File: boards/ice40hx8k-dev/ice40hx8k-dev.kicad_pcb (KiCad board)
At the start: 4 copper layers, 35 x 30 mm, 33 parts, among them U1 ICE40HX8K-CT256

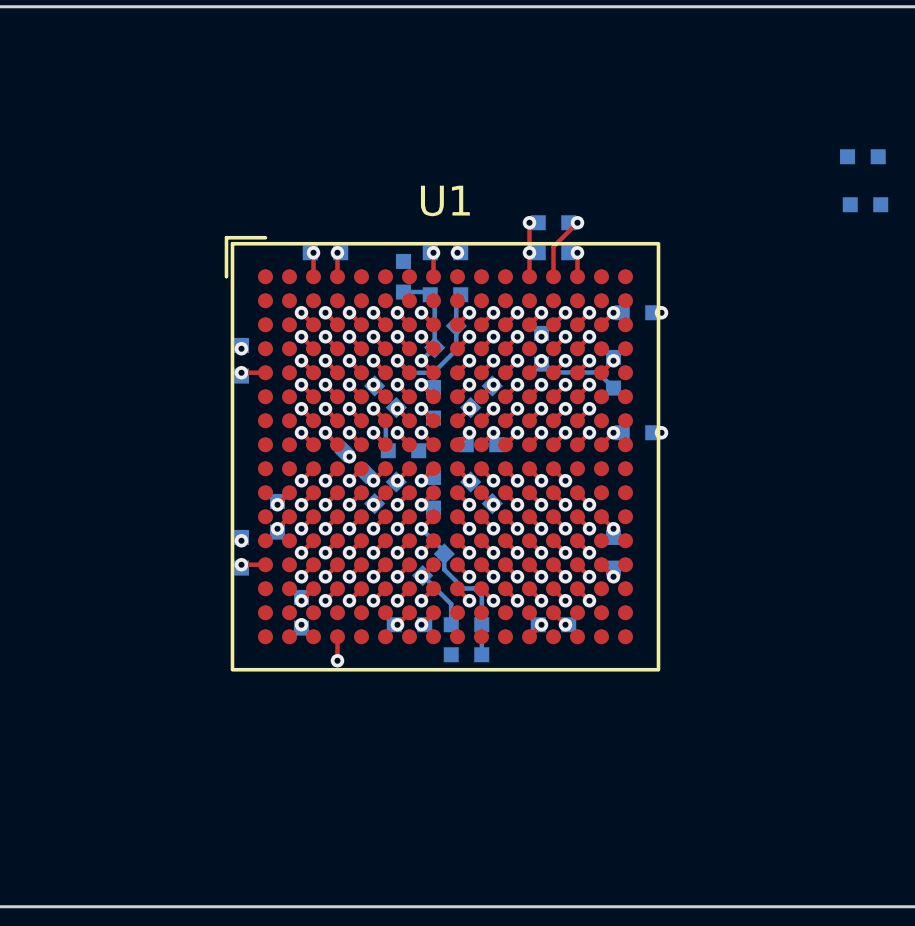
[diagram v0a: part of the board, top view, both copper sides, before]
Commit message: Fan out all signal pads.
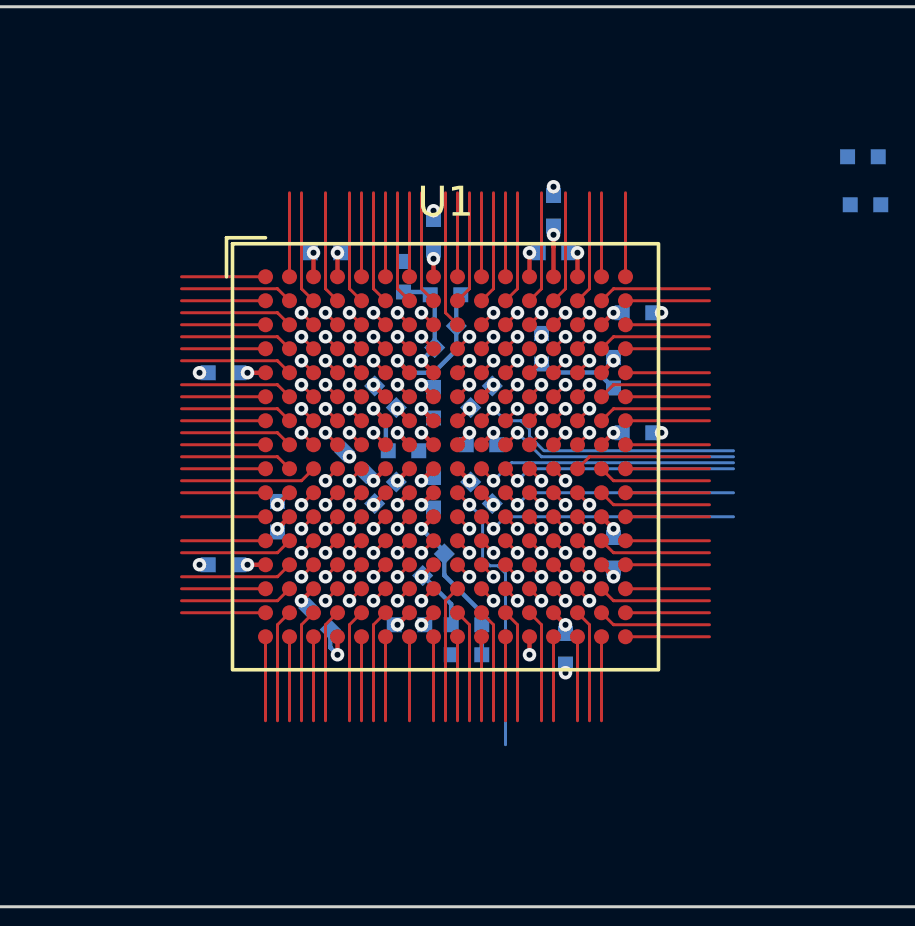
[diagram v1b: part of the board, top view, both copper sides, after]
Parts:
- moved C17 0.89 mm to (142.0, 91.4), turned to -90 degrees
- moved C24 0.72 mm to (137.6, 77.6), turned to 90 degrees
- moved C12 0.72 mm to (130.6, 82.2), turned to 180 degrees
- moved C13 0.72 mm to (130.6, 88.6), turned to 180 degrees
- moved C16 0.63 mm to (133.8, 90.4), turned to -45 degrees
- moved C25 0.40 mm to (141.6, 76.8), turned to 90 degrees
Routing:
- net unconnected-(U1-PadL6): track 0.57 -> 10.1 mm
- net unconnected-(U1-PadF5): track 0.57 -> 9.93 mm
- net unconnected-(U1-PadG10): track 0.57 -> 9.28 mm
- net unconnected-(U1-PadK9): track 0.57 -> 9.22 mm
- net unconnected-(U1-PadF7): track 0.57 -> 9.21 mm
- net unconnected-(U1-PadJ10): track 0.57 -> 8.81 mm
- net unconnected-(U1-PadL10): track 0.57 -> 8.73 mm
- net unconnected-(U1-PadL7): track 0.57 -> 8.50 mm
- net unconnected-(U1-PadL11): track 0.57 -> 8.45 mm
- net unconnected-(U1-PadG11): track 0.57 -> 8.38 mm
- net unconnected-(U1-PadE6): track 0.57 -> 8.33 mm
- net unconnected-(U1-PadF12): track 0.57 -> 8.21 mm
- net unconnected-(U1-PadH11): track 0.57 -> 8.10 mm
- net unconnected-(U1-PadM11): track 0.57 -> 8.08 mm
- net unconnected-(U1-PadK11): track 0.57 -> 7.93 mm
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
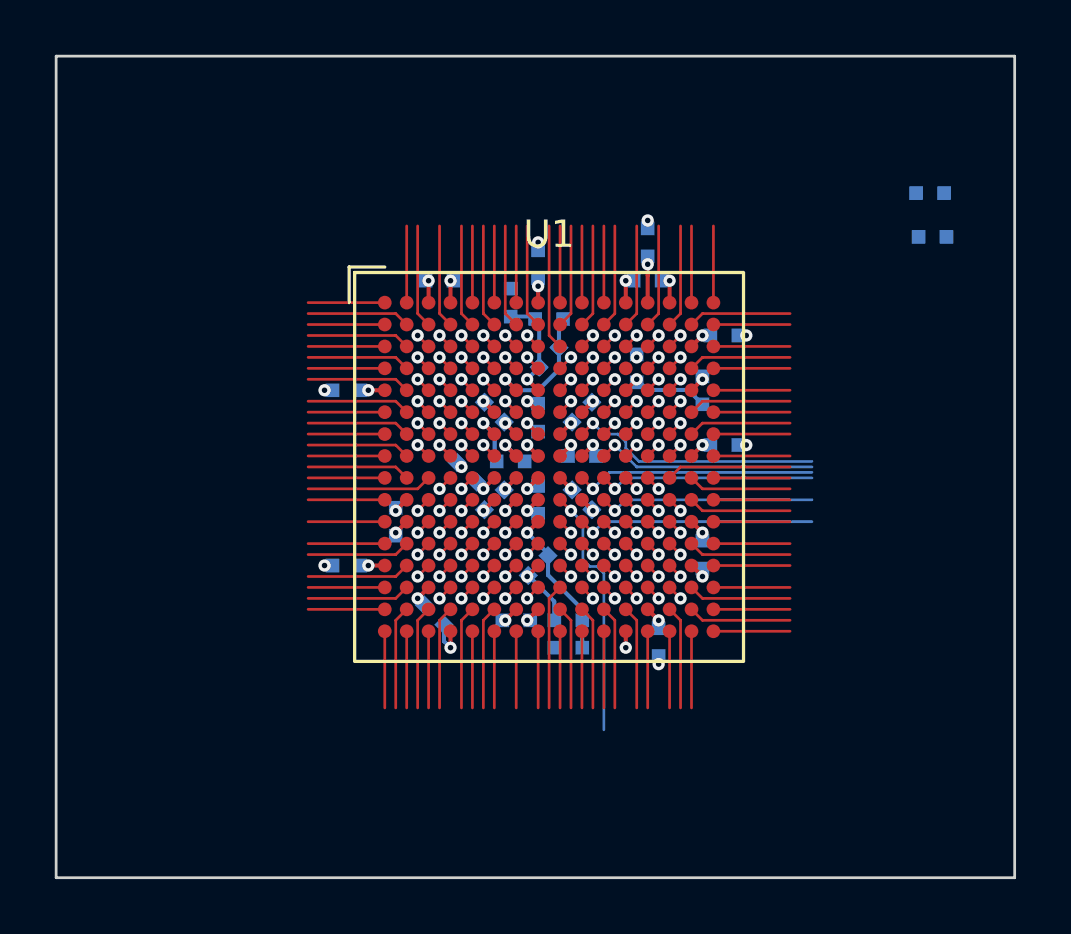
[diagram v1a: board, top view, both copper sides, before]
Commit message: Split up schematic and label all nets.
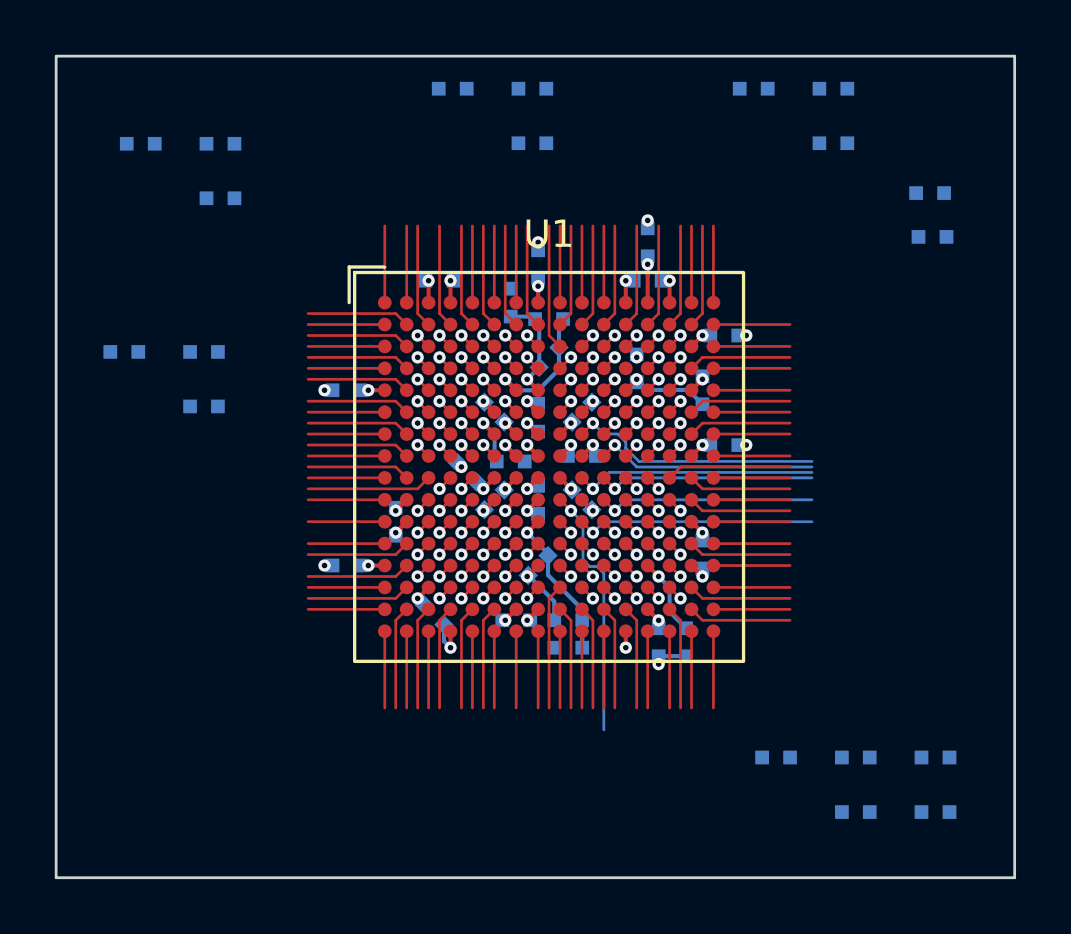
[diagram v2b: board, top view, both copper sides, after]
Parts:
- added C31: 100n, 0Local:C_SMD_0402_Pad0.5mm, B.Cu at (143.0, 91.4)
- added C32: 10n, 0Local:C_SMD_0402_Pad0.5mm, B.Cu at (149.2, 95.6)
- added C33: 10n, 0Local:C_SMD_0402_Pad0.5mm, B.Cu at (149.2, 97.6)
- added C34: 1u, 0Local:C_SMD_0402_Pad0.5mm, B.Cu at (146.3, 95.6)
- added C35: 10n, 0Local:C_SMD_0402_Pad0.5mm, B.Cu at (126.0, 73.2)
- added C36: 1u, 0Local:C_SMD_0402_Pad0.5mm, B.Cu at (126.0, 75.2)
- added C37: 10u, 0Local:C_SMD_0402_Pad0.5mm, B.Cu at (123.1, 73.2)
- added C38: 10n, 0Local:C_SMD_0402_Pad0.5mm, B.Cu at (125.4, 80.8)
- added C39: 1u, 0Local:C_SMD_0402_Pad0.5mm, B.Cu at (125.4, 82.8)
- added C40: 100n, 0Local:C_SMD_0402_Pad0.5mm, B.Cu at (122.5, 80.8)
- added C41: 10n, 0Local:C_SMD_0402_Pad0.5mm, B.Cu at (145.5, 71.2)
- added C42: 1u, 0Local:C_SMD_0402_Pad0.5mm, B.Cu at (148.4, 73.2)
- added C43: 10u, 0Local:C_SMD_0402_Pad0.5mm, B.Cu at (148.4, 71.2)
- added C44: 10n, 0Local:C_SMD_0402_Pad0.5mm, B.Cu at (137.4, 71.2)
- added C45: 1u, 0Local:C_SMD_0402_Pad0.5mm, B.Cu at (137.4, 73.2)
- added C46: 10u, 0Local:C_SMD_0402_Pad0.5mm, B.Cu at (134.5, 71.2)
- added R3: 0R, 0Local:R_SMD_0402_Pad0.5mm, B.Cu at (152.1, 95.6)
- added R4: 0R, 0Local:R_SMD_0402_Pad0.5mm, B.Cu at (152.1, 97.6)
- C1: value 10u -> 100n
- C3: value 100n -> 10u
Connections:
- net +2V5 renamed /Power/VPP_2V5
- net /VCCIO_0 renamed /IO_Bank_0/VCCIO_0
- net /VCCIO_1 renamed /IO_Bank_1/VCCIO_1
- net /VCCIO_2 renamed /IO_Bank_2/VCCIO_2
- net /VCCIO_3 renamed /IO_Bank_3/VCCIO_0
- C10 pad 1: +1V2 -> /Power/VCC
- C27 pad 1: +1V2 -> /Power/VCC
- C28 pad 1: +1V2 -> /Power/VCC
- C5 pad 1: +1V2 -> /Power/VCC
- C6 pad 1: +1V2 -> /Power/VCC
- C7 pad 1: +1V2 -> /Power/VCC
- C8 pad 1: +1V2 -> /Power/VCC
- C9 pad 1: +1V2 -> /Power/VCC
- U1 pad A1: unconnected-(U1-PadA1) -> /IO_Bank_0/IO0_220
- U1 pad A10: unconnected-(U1-PadA10) -> /IO_Bank_0/IO0_186
- U1 pad A11: unconnected-(U1-PadA11) -> /IO_Bank_0/IO0_187
- U1 pad A14: +1V2 -> /Power/VCC
- U1 pad A15: unconnected-(U1-PadA15) -> /IO_Bank_0/IO0_177
- U1 pad A16: unconnected-(U1-PadA16) -> /IO_Bank_0/IO0_176
- U1 pad A2: unconnected-(U1-PadA2) -> /IO_Bank_0/IO0_218
- U1 pad A5: unconnected-(U1-PadA5) -> /IO_Bank_0/IO0_213
- U1 pad A6: unconnected-(U1-PadA6) -> /IO_Bank_0/IO0_211
- U1 pad A7: unconnected-(U1-PadA7) -> /IO_Bank_0/IO0_205
- U1 pad A9: unconnected-(U1-PadA9) -> /IO_Bank_0/IO0_194
- U1 pad B1: unconnected-(U1-PadB1) -> /IO_Bank_3/IO3_2_P
- U1 pad B10: unconnected-(U1-PadB10) -> /IO_Bank_0/IO0_183
- U1 pad B11: unconnected-(U1-PadB11) -> /IO_Bank_0/IO0_184
- U1 pad B12: unconnected-(U1-PadB12) -> /IO_Bank_0/IO0_182
- U1 pad B13: unconnected-(U1-PadB13) -> /IO_Bank_0/IO0_178
- U1 pad B14: unconnected-(U1-PadB14) -> /IO_Bank_0/IO0_171
- U1 pad B15: unconnected-(U1-PadB15) -> /IO_Bank_0/IO0_169
- U1 pad B16: unconnected-(U1-PadB16) -> /IO_Bank_1/IO1_165
- U1 pad B2: unconnected-(U1-PadB2) -> /IO_Bank_3/IO3_1_P
- U1 pad B3: unconnected-(U1-PadB3) -> /IO_Bank_0/IO0_223
- U1 pad B4: unconnected-(U1-PadB4) -> /IO_Bank_0/IO0_216
- U1 pad B5: unconnected-(U1-PadB5) -> /IO_Bank_0/IO0_214
- U1 pad B6: unconnected-(U1-PadB6) -> /IO_Bank_0/IO0_208
- U1 pad B7: unconnected-(U1-PadB7) -> /IO_Bank_0/IO0_207
- U1 pad B8: unconnected-(U1-PadB8) -> /IO_Bank_0/IO0_203
- U1 pad B9: unconnected-(U1-PadB9) -> /IO_Bank_0/IO0_199
- U1 pad C1: unconnected-(U1-PadC1) -> /IO_Bank_3/IO3_3_N
- U1 pad C10: unconnected-(U1-PadC10) -> /IO_Bank_0/IO0_185
- U1 pad C11: unconnected-(U1-PadC11) -> /IO_Bank_0/IO0_180
- U1 pad C12: unconnected-(U1-PadC12) -> /IO_Bank_0/IO0_172
- U1 pad C13: unconnected-(U1-PadC13) -> /IO_Bank_0/IO0_174
- U1 pad C14: unconnected-(U1-PadC14) -> /IO_Bank_0/IO0_168
- U1 pad C16: unconnected-(U1-PadC16) -> /IO_Bank_1/IO1_161
- U1 pad C2: unconnected-(U1-PadC2) -> /IO_Bank_3/IO3_3_P
- U1 pad C3: unconnected-(U1-PadC3) -> /IO_Bank_0/IO0_227
- U1 pad C4: unconnected-(U1-PadC4) -> /IO_Bank_0/IO0_222
- U1 pad C5: unconnected-(U1-PadC5) -> /IO_Bank_0/IO0_221
- U1 pad C6: unconnected-(U1-PadC6) -> /IO_Bank_0/IO0_209
- U1 pad C7: unconnected-(U1-PadC7) -> /IO_Bank_0/IO0_206
- U1 pad C8: unconnected-(U1-PadC8) -> /IO_Bank_0/IO0_197
- U1 pad C9: unconnected-(U1-PadC9) -> /IO_Bank_0/IO0_191
- U1 pad D1: unconnected-(U1-PadD1) -> /IO_Bank_3/IO3_5_P
- U1 pad D10: unconnected-(U1-PadD10) -> /IO_Bank_0/IO0_190
- U1 pad D11: unconnected-(U1-PadD11) -> /IO_Bank_0/IO0_181
- U1 pad D13: unconnected-(U1-PadD13) -> /IO_Bank_0/IO0_170
- U1 pad D14: unconnected-(U1-PadD14) -> /IO_Bank_1/IO1_167
- U1 pad D15: unconnected-(U1-PadD15) -> /IO_Bank_1/IO1_157
- U1 pad D16: unconnected-(U1-PadD16) -> /IO_Bank_1/IO1_153
- U1 pad D2: unconnected-(U1-PadD2) -> /IO_Bank_3/IO3_4_P
- U1 pad D3: unconnected-(U1-PadD3) -> /IO_Bank_0/IO0_226
- U1 pad D4: unconnected-(U1-PadD4) -> /IO_Bank_0/IO0_224
- U1 pad D5: unconnected-(U1-PadD5) -> /IO_Bank_0/IO0_219
- U1 pad D6: unconnected-(U1-PadD6) -> /IO_Bank_0/IO0_212
- U1 pad D7: unconnected-(U1-PadD7) -> /IO_Bank_0/IO0_210
- U1 pad D8: unconnected-(U1-PadD8) -> /IO_Bank_0/IO0_200
- U1 pad D9: unconnected-(U1-PadD9) -> /IO_Bank_0/IO0_193
- U1 pad E10: unconnected-(U1-PadE10) -> /IO_Bank_0/IO0_179
- U1 pad E11: unconnected-(U1-PadE11) -> /IO_Bank_0/IO0_173
- U1 pad E13: unconnected-(U1-PadE13) -> /IO_Bank_1/IO1_166
- U1 pad E14: unconnected-(U1-PadE14) -> /IO_Bank_1/IO1_160
- U1 pad E16: unconnected-(U1-PadE16) -> /IO_Bank_1/IO1_151
- U1 pad E2: unconnected-(U1-PadE2) -> /IO_Bank_3/IO3_7_P
- U1 pad E3: unconnected-(U1-PadE3) -> /IO_Bank_3/IO3_6_P
- U1 pad E4: unconnected-(U1-PadE4) -> /IO_Bank_3/IO3_1_N
- U1 pad E5: unconnected-(U1-PadE5) -> /IO_Bank_0/IO0_225
- U1 pad E6: unconnected-(U1-PadE6) -> /IO_Bank_0/IO0_215
- U1 pad E9: unconnected-(U1-PadE9) -> /IO_Bank_0/IO0_192
- U1 pad F1: unconnected-(U1-PadF1) -> /IO_Bank_3/IO3_10_P
- U1 pad F10: +1V2 -> /Power/VCC
- U1 pad F11: unconnected-(U1-PadF11) -> /IO_Bank_1/IO1_158
- U1 pad F12: unconnected-(U1-PadF12) -> /IO_Bank_1/IO1_156
- U1 pad F13: unconnected-(U1-PadF13) -> /IO_Bank_1/IO1_162
- U1 pad F14: unconnected-(U1-PadF14) -> /IO_Bank_1/IO1_155
- U1 pad F15: unconnected-(U1-PadF15) -> /IO_Bank_1/IO1_149
- U1 pad F16: unconnected-(U1-PadF16) -> /IO_Bank_1/IO1_147
- U1 pad F2: unconnected-(U1-PadF2) -> /IO_Bank_3/IO3_9_P
- U1 pad F3: unconnected-(U1-PadF3) -> /IO_Bank_3/IO3_8_P
- U1 pad F4: unconnected-(U1-PadF4) -> /IO_Bank_3/IO3_4_N
- U1 pad F5: unconnected-(U1-PadF5) -> /IO_Bank_3/IO3_2_N
- U1 pad F6: +1V2 -> /Power/VCC
- U1 pad F7: unconnected-(U1-PadF7) -> /IO_Bank_0/IO0_198
- U1 pad F9: unconnected-(U1-PadF9) -> /IO_Bank_0/IO0_196
- U1 pad G1: unconnected-(U1-PadG1) -> /IO_Bank_3/IO3_13_P
- U1 pad G10: unconnected-(U1-PadG10) -> /IO_Bank_1/IO1_146
- U1 pad G11: unconnected-(U1-PadG11) -> /IO_Bank_1/IO1_148
- U1 pad G12: unconnected-(U1-PadG12) -> /IO_Bank_1/IO1_154
- U1 pad G13: unconnected-(U1-PadG13) -> /IO_Bank_1/IO1_152
- U1 pad G14: unconnected-(U1-PadG14) -> /IO_Bank_1/IO1_150
- U1 pad G15: unconnected-(U1-PadG15) -> /IO_Bank_1/IO1_145
- U1 pad G16: unconnected-(U1-PadG16) -> /IO_Bank_1/IO1_143
- U1 pad G2: unconnected-(U1-PadG2) -> /IO_Bank_3/IO3_11_P
- U1 pad G3: unconnected-(U1-PadG3) -> /IO_Bank_3/IO3_8_N
- U1 pad G4: unconnected-(U1-PadG4) -> /IO_Bank_3/IO3_6_N
- U1 pad G5: unconnected-(U1-PadG5) -> /IO_Bank_3/IO3_5_N
- U1 pad H1: unconnected-(U1-PadH1) -> /IO_Bank_3/IO3_14_P
- U1 pad H11: unconnected-(U1-PadH11) -> /IO_Bank_1/IO1_140
- U1 pad H12: unconnected-(U1-PadH12) -> /IO_Bank_1/IO1_144
- U1 pad H13: unconnected-(U1-PadH13) -> /IO_Bank_1/IO1_139
- U1 pad H14: unconnected-(U1-PadH14) -> /IO_Bank_1/IO1_142
- U1 pad H16: unconnected-(U1-PadH16) -> /IO_Bank_1/IO1_141
- U1 pad H2: unconnected-(U1-PadH2) -> /IO_Bank_3/IO3_12_P
- U1 pad H3: unconnected-(U1-PadH3) -> /IO_Bank_3/IO3_9_N
- U1 pad H4: unconnected-(U1-PadH4) -> /IO_Bank_3/IO3_11_N
- U1 pad H5: unconnected-(U1-PadH5) -> /IO_Bank_3/IO3_7_N
- U1 pad H6: unconnected-(U1-PadH6) -> /IO_Bank_3/IO3_10_N
- U1 pad J1: unconnected-(U1-PadJ1) -> /IO_Bank_3/IO3_15_P
- U1 pad J10: unconnected-(U1-PadJ10) -> /IO_Bank_1/IO1_122
- U1 pad J11: unconnected-(U1-PadJ11) -> /IO_Bank_1/IO1_126
- U1 pad J12: unconnected-(U1-PadJ12) -> /IO_Bank_1/IO1_136
- U1 pad J13: unconnected-(U1-PadJ13) -> /IO_Bank_1/IO1_137
- U1 pad J14: unconnected-(U1-PadJ14) -> /IO_Bank_1/IO1_134
- U1 pad J15: unconnected-(U1-PadJ15) -> /IO_Bank_1/IO1_130
- U1 pad J16: unconnected-(U1-PadJ16) -> /IO_Bank_1/IO1_138
- U1 pad J2: unconnected-(U1-PadJ2) -> /IO_Bank_3/IO3_15_N
- U1 pad J3: unconnected-(U1-PadJ3) -> /IO_Bank_3/IO3_14_N
- U1 pad J4: unconnected-(U1-PadJ4) -> /IO_Bank_3/IO3_12_N
- U1 pad J5: unconnected-(U1-PadJ5) -> /IO_Bank_3/IO3_13_N
- U1 pad K1: unconnected-(U1-PadK1) -> /IO_Bank_3/IO3_16_N
- U1 pad K10: +1V2 -> /Power/VCC
- U1 pad K11: unconnected-(U1-PadK11) -> /IO_Bank_2/IO2_103
- U1 pad K12: unconnected-(U1-PadK12) -> /IO_Bank_1/IO1_120
- U1 pad K13: unconnected-(U1-PadK13) -> /IO_Bank_1/IO1_128
- U1 pad K14: unconnected-(U1-PadK14) -> /IO_Bank_1/IO1_129
- U1 pad K15: unconnected-(U1-PadK15) -> /IO_Bank_1/IO1_131
- U1 pad K16: unconnected-(U1-PadK16) -> /IO_Bank_1/IO1_133
- U1 pad K3: unconnected-(U1-PadK3) -> /IO_Bank_3/IO3_16_P
- U1 pad K4: unconnected-(U1-PadK4) -> /IO_Bank_3/IO3_18_N
- U1 pad K5: unconnected-(U1-PadK5) -> /IO_Bank_3/IO3_20_N
- U1 pad K6: +1V2 -> /Power/VCC
- U1 pad K9: unconnected-(U1-PadK9) -> /IO_Bank_2/IO2_82
- U1 pad L1: unconnected-(U1-PadL1) -> /IO_Bank_3/IO3_17_P
- U1 pad L10: unconnected-(U1-PadL10) -> /IO_Bank_2/IO2_85
- U1 pad L11: unconnected-(U1-PadL11) -> /IO_Bank_2/IO2_99
- U1 pad L12: unconnected-(U1-PadL12) -> /IO_Bank_1/IO1_116
- U1 pad L13: unconnected-(U1-PadL13) -> /IO_Bank_1/IO1_118
- U1 pad L14: unconnected-(U1-PadL14) -> /IO_Bank_1/IO1_119
- U1 pad L16: unconnected-(U1-PadL16) -> /IO_Bank_1/IO1_127
- U1 pad L2: +1V2 -> /Power/VCC
- U1 pad L3: unconnected-(U1-PadL3) -> /IO_Bank_3/IO3_19_P
- U1 pad L4: unconnected-(U1-PadL4) -> /IO_Bank_3/IO3_17_N
- U1 pad L5: unconnected-(U1-PadL5) -> /IO_Bank_3/IO3_23_N
- U1 pad L6: unconnected-(U1-PadL6) -> /IO_Bank_3/IO3_19_N
- U1 pad L7: unconnected-(U1-PadL7) -> /IO_Bank_3/IO3_21_N
- U1 pad L9: unconnected-(U1-PadL9) -> /IO_Bank_2/IO2_74
- U1 pad M1: unconnected-(U1-PadM1) -> /IO_Bank_3/IO3_18_P
- U1 pad M10: unconnected-(U1-PadM10) -> /USB_Config/CFG_DONE
- U1 pad M11: unconnected-(U1-PadM11) -> /IO_Bank_2/IO2_93
- U1 pad M12: unconnected-(U1-PadM12) -> /IO_Bank_2/IO2_101
- U1 pad M13: unconnected-(U1-PadM13) -> /IO_Bank_1/IO1_114
- U1 pad M14: unconnected-(U1-PadM14) -> /IO_Bank_1/IO1_115
- U1 pad M15: unconnected-(U1-PadM15) -> /IO_Bank_1/IO1_123
- U1 pad M16: unconnected-(U1-PadM16) -> /IO_Bank_1/IO1_121
- U1 pad M2: unconnected-(U1-PadM2) -> /IO_Bank_3/IO3_20_P
- U1 pad M3: unconnected-(U1-PadM3) -> /IO_Bank_3/IO3_22_P
- U1 pad M4: unconnected-(U1-PadM4) -> /IO_Bank_3/IO3_24_P
- U1 pad M5: unconnected-(U1-PadM5) -> /IO_Bank_3/IO3_25_P
- U1 pad M6: unconnected-(U1-PadM6) -> /IO_Bank_3/IO3_22_N
- U1 pad M7: unconnected-(U1-PadM7) -> /IO_Bank_2/IO2_64
- U1 pad M8: unconnected-(U1-PadM8) -> /IO_Bank_2/IO2_68
- U1 pad M9: unconnected-(U1-PadM9) -> /IO_Bank_2/IO2_80
- U1 pad N10: unconnected-(U1-PadN10) -> /IO_Bank_2/IO2_87
- U1 pad N11: unconnected-(U1-PadN11) -> /USB_Config/CFG_~{RESET}
- U1 pad N12: unconnected-(U1-PadN12) -> /IO_Bank_2/IO2_98
- U1 pad N13: unconnected-(U1-PadN13) -> /USB_Config/VCCIO_2
- U1 pad N16: unconnected-(U1-PadN16) -> /IO_Bank_1/IO1_117
- U1 pad N2: unconnected-(U1-PadN2) -> /IO_Bank_3/IO3_21_P
- U1 pad N3: unconnected-(U1-PadN3) -> /IO_Bank_3/IO3_23_P
- U1 pad N4: unconnected-(U1-PadN4) -> /IO_Bank_3/IO3_26_P
- U1 pad N5: unconnected-(U1-PadN5) -> /IO_Bank_2/IO2_56
- U1 pad N6: unconnected-(U1-PadN6) -> /IO_Bank_2/IO2_52
- U1 pad N7: unconnected-(U1-PadN7) -> /IO_Bank_2/IO2_66
- U1 pad N9: unconnected-(U1-PadN9) -> /IO_Bank_2/IO2_78
- U1 pad P1: unconnected-(U1-PadP1) -> /IO_Bank_3/IO3_24_N
- U1 pad P10: unconnected-(U1-PadP10) -> /IO_Bank_2/IO2_86
- U1 pad P11: unconnected-(U1-PadP11) -> /USB_Config/CFG_SDI
- U1 pad P12: unconnected-(U1-PadP12) -> /USB_Config/CFG_SDO
- U1 pad P13: unconnected-(U1-PadP13) -> /IO_Bank_2/IO2_104
- U1 pad P14: unconnected-(U1-PadP14) -> /IO_Bank_1/IO1_111
- U1 pad P15: unconnected-(U1-PadP15) -> /IO_Bank_1/IO1_112
- U1 pad P16: unconnected-(U1-PadP16) -> /IO_Bank_1/IO1_113
- U1 pad P2: unconnected-(U1-PadP2) -> /IO_Bank_3/IO3_25_N
- U1 pad P4: unconnected-(U1-PadP4) -> /IO_Bank_2/IO2_54
- U1 pad P5: unconnected-(U1-PadP5) -> /IO_Bank_2/IO2_58
- U1 pad P6: unconnected-(U1-PadP6) -> /IO_Bank_2/IO2_67
- U1 pad P7: unconnected-(U1-PadP7) -> /IO_Bank_2/IO2_77
- U1 pad P8: unconnected-(U1-PadP8) -> /IO_Bank_2/IO2_72
- U1 pad P9: unconnected-(U1-PadP9) -> /IO_Bank_2/IO2_83
- U1 pad R1: unconnected-(U1-PadR1) -> /IO_Bank_3/IO3_26_N
- U1 pad R10: unconnected-(U1-PadR10) -> /IO_Bank_2/IO2_84
- U1 pad R11: unconnected-(U1-PadR11) -> /USB_Config/CFG_SCK
- U1 pad R12: unconnected-(U1-PadR12) -> /USB_Config/CFG_~{SSEL}
- U1 pad R14: unconnected-(U1-PadR14) -> /IO_Bank_1/IO1_109
- U1 pad R15: unconnected-(U1-PadR15) -> /IO_Bank_1/IO1_110
- U1 pad R16: unconnected-(U1-PadR16) -> /IO_Bank_2/IO2_102
- U1 pad R2: unconnected-(U1-PadR2) -> /IO_Bank_2/IO2_55
- U1 pad R3: unconnected-(U1-PadR3) -> /IO_Bank_2/IO2_59
- U1 pad R4: unconnected-(U1-PadR4) -> /IO_Bank_2/IO2_63
- U1 pad R5: unconnected-(U1-PadR5) -> /IO_Bank_2/IO2_60
- U1 pad R6: unconnected-(U1-PadR6) -> /IO_Bank_2/IO2_71
- U1 pad R9: unconnected-(U1-PadR9) -> /IO_Bank_2/IO2_81
- U1 pad T1: unconnected-(U1-PadT1) -> /IO_Bank_2/IO2_53
- U1 pad T10: unconnected-(U1-PadT10) -> /IO_Bank_2/IO2_88
- U1 pad T11: unconnected-(U1-PadT11) -> /IO_Bank_2/IO2_89
- U1 pad T13: unconnected-(U1-PadT13) -> /IO_Bank_2/IO2_94
- U1 pad T14: unconnected-(U1-PadT14) -> /IO_Bank_2/IO2_92
- U1 pad T15: unconnected-(U1-PadT15) -> /IO_Bank_2/IO2_91
- U1 pad T16: unconnected-(U1-PadT16) -> /IO_Bank_2/IO2_100
- U1 pad T2: unconnected-(U1-PadT2) -> /IO_Bank_2/IO2_57
- U1 pad T3: unconnected-(U1-PadT3) -> /IO_Bank_2/IO2_61
- U1 pad T5: unconnected-(U1-PadT5) -> /IO_Bank_2/IO2_69
- U1 pad T6: unconnected-(U1-PadT6) -> /IO_Bank_2/IO2_73
- U1 pad T7: unconnected-(U1-PadT7) -> /IO_Bank_2/IO2_75
- U1 pad T8: unconnected-(U1-PadT8) -> /IO_Bank_2/IO2_76
- U1 pad T9: unconnected-(U1-PadT9) -> /IO_Bank_2/IO2_79
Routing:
- net unconnected-(U1-PadL6): track 10.1 -> 0.00 mm, vias 1 -> 0
- net /IO_Bank_3/IO3_19_N: track 0.00 -> 10.1 mm, vias 0 -> 1
- net unconnected-(U1-PadF5): track 9.93 -> 0.00 mm, vias 1 -> 0
- net /IO_Bank_3/IO3_2_N: track 0.00 -> 9.93 mm, vias 0 -> 1
- net unconnected-(U1-PadG10): track 9.28 -> 0.00 mm, vias 1 -> 0
- net /IO_Bank_1/IO1_146: track 0.00 -> 9.28 mm, vias 0 -> 1
- net unconnected-(U1-PadK9): track 9.22 -> 0.00 mm, vias 1 -> 0
- net /IO_Bank_2/IO2_82: track 0.00 -> 9.22 mm, vias 0 -> 1
- net unconnected-(U1-PadF7): track 9.21 -> 0.00 mm, vias 1 -> 0
- net /IO_Bank_0/IO0_198: track 0.00 -> 9.21 mm, vias 0 -> 1
- net unconnected-(U1-PadJ10): track 8.81 -> 0.00 mm, vias 1 -> 0
- net /IO_Bank_1/IO1_122: track 0.00 -> 8.81 mm, vias 0 -> 1
- net unconnected-(U1-PadL10): track 8.73 -> 0.00 mm, vias 1 -> 0
- net /IO_Bank_2/IO2_85: track 0.00 -> 8.73 mm, vias 0 -> 1
- net unconnected-(U1-PadL7): track 8.50 -> 0.00 mm, vias 1 -> 0
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
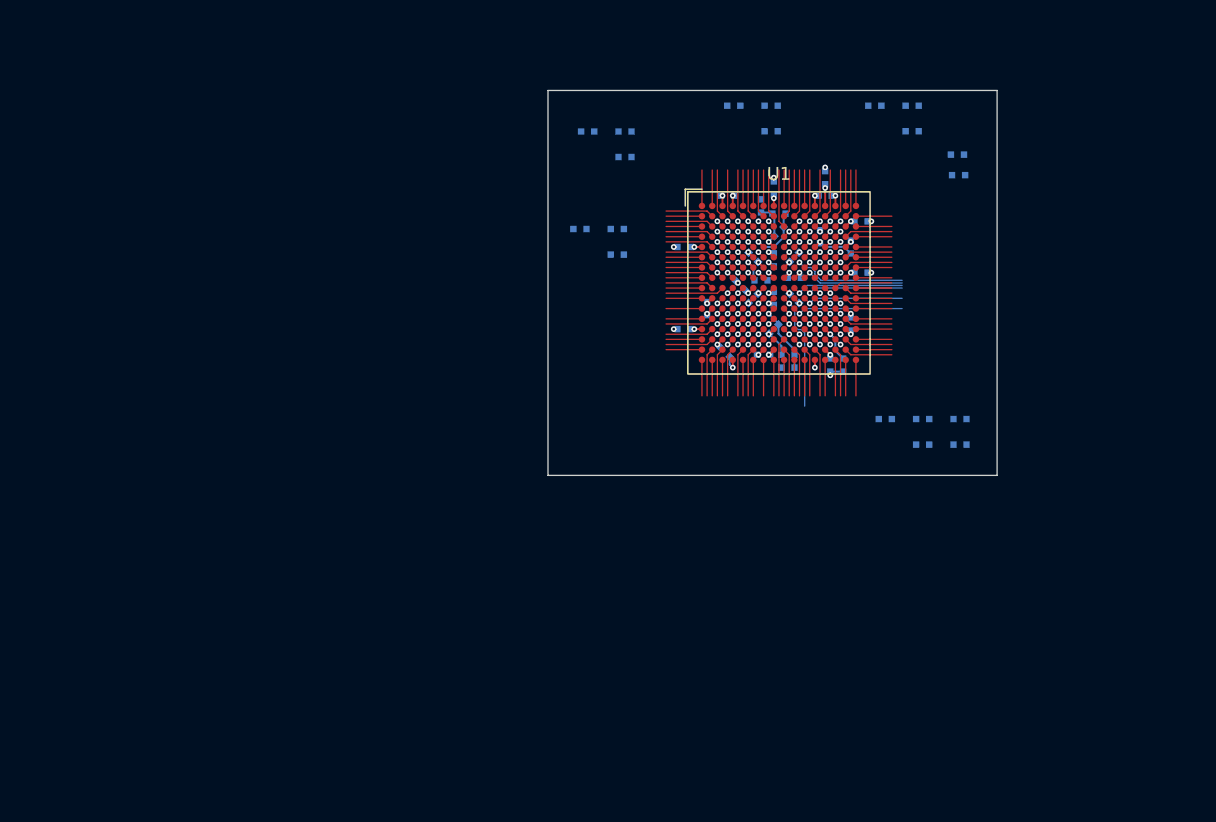
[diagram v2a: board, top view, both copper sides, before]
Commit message: Switch to 6 layers, add power fills under BGA.
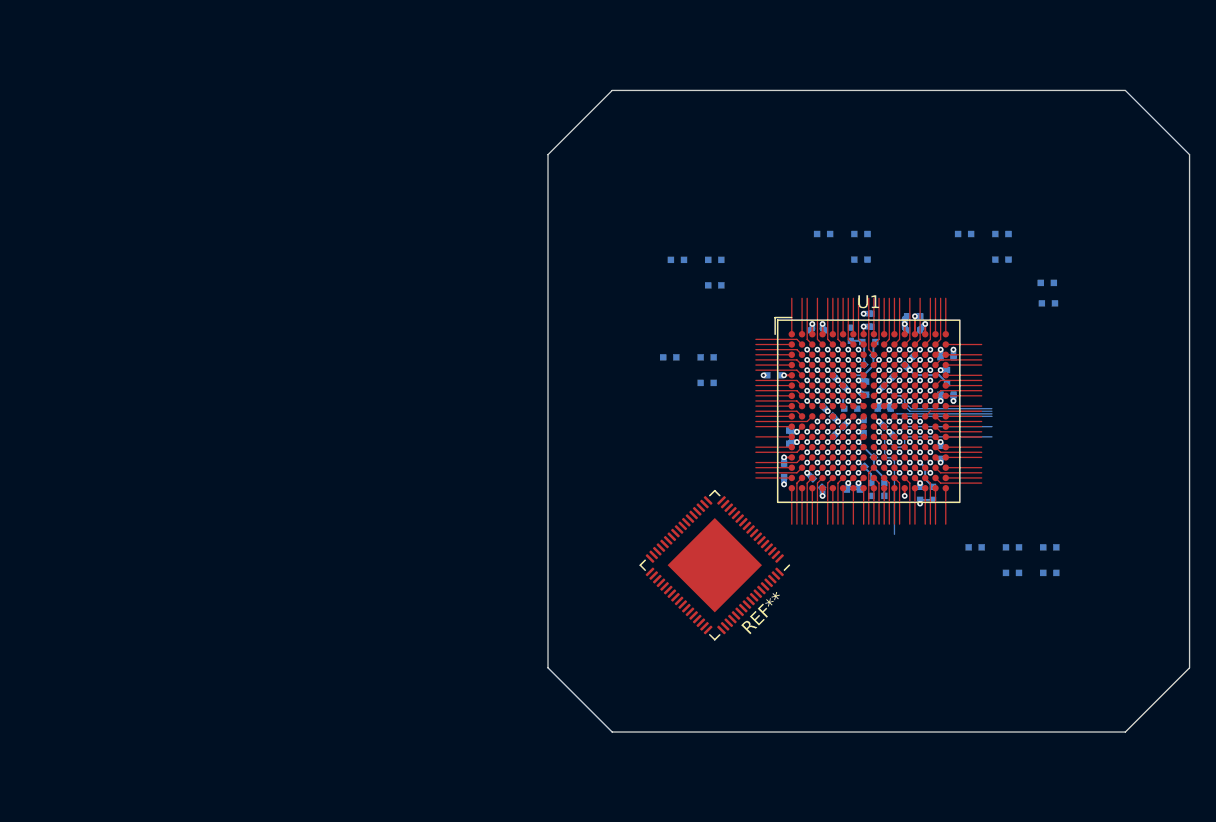
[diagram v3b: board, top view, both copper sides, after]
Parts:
- added REF**: FT2232HPQ, Package_DFN_QFN:QFN-68-1EP_8x8mm_P0.4mm_EP5.2x5.2mm, F.Cu at (133.0, 107.0)
- moved C13 13.5 mm to (138.4, 99.6), turned to -90 degrees
- moved C25 12.8 mm to (148.5, 87.6), turned to 180 degrees
- moved C24 12.8 mm to (145.2, 87.9)
- moved C3 12.8 mm to (145.0, 99.0)
- moved C10 12.7 mm to (146.6, 96.6)
- moved C15 12.6 mm to (143.8, 101.1)
- moved C23 12.6 mm to (141.0, 88.7)
- moved C29 12.6 mm to (151.1, 92.3)
- moved C27 12.6 mm to (148.5, 88.7)
- moved C20 12.5 mm to (151.1, 90.8)
- moved C16 12.5 mm to (141.0, 100.6)
- moved C22 12.4 mm to (146.2, 94.8)
- moved C26 12.3 mm to (144.8, 93.2)
- moved C8 12.3 mm to (142.6, 96.6)
- moved C40 12.2 mm to (129.5, 90.8)
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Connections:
- net /IO_Bank_3/VCCIO_0 renamed /IO_Bank_3/VCCIO_3
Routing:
- net GND: track 15.0 -> 24.2 mm, vias 27 -> 26
- net /Power/VCC: track 3.63 -> 7.11 mm
- net /IO_Bank_0/VCCIO_0: track 3.37 -> 5.56 mm
- net /IO_Bank_1/VCCIO_1: track 2.26 -> 4.02 mm
- net /IO_Bank_2/VCCIO_2: track 2.26 -> 3.43 mm
- net /Power/VPP_2V5: track 3.34 -> 4.45 mm
- net /IO_Bank_3/VCCIO_3: track 3.93 -> 4.99 mm
- net /IO_Bank_2/IO2_85: track 8.73 -> 9.29 mm
- added copper zone on In3.Cu, net /IO_Bank_0/VCCIO_0
- added copper zone on In3.Cu, net /IO_Bank_1/VCCIO_1
- added copper zone on In3.Cu, net /IO_Bank_2/VCCIO_2
- added copper zone on In3.Cu, net /IO_Bank_3/VCCIO_3
- added copper zone on In3.Cu, net /Power/VCC
- added copper zone on In4.Cu, net GND
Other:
- board size 35 x 30 mm -> 50 x 50 mm
- copper layers 4 -> 6
